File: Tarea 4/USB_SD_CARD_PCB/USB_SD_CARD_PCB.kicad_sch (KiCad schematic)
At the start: 3 parts

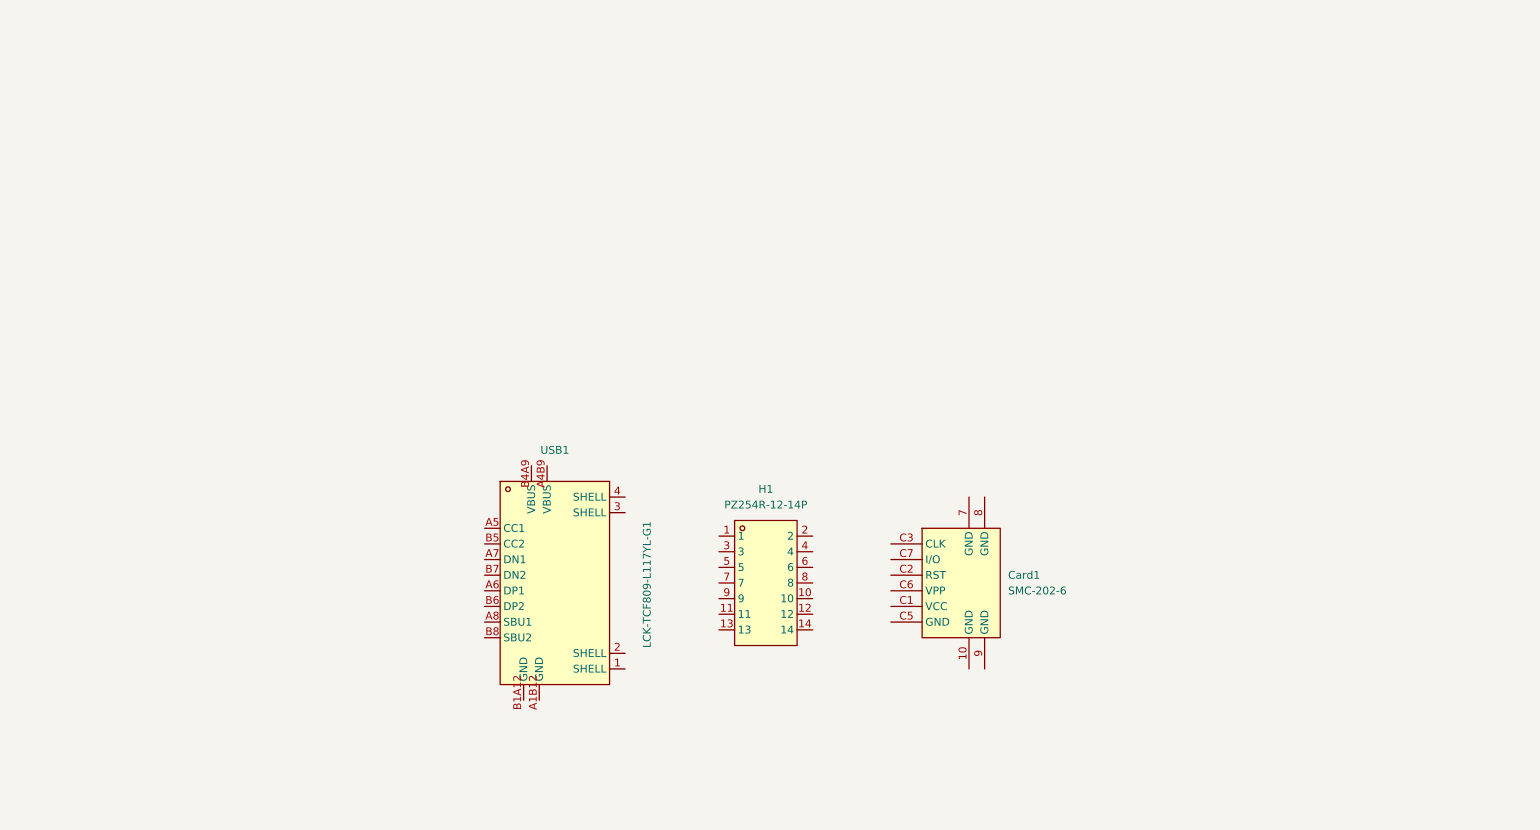
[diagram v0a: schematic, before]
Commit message: USB type c Conexiones
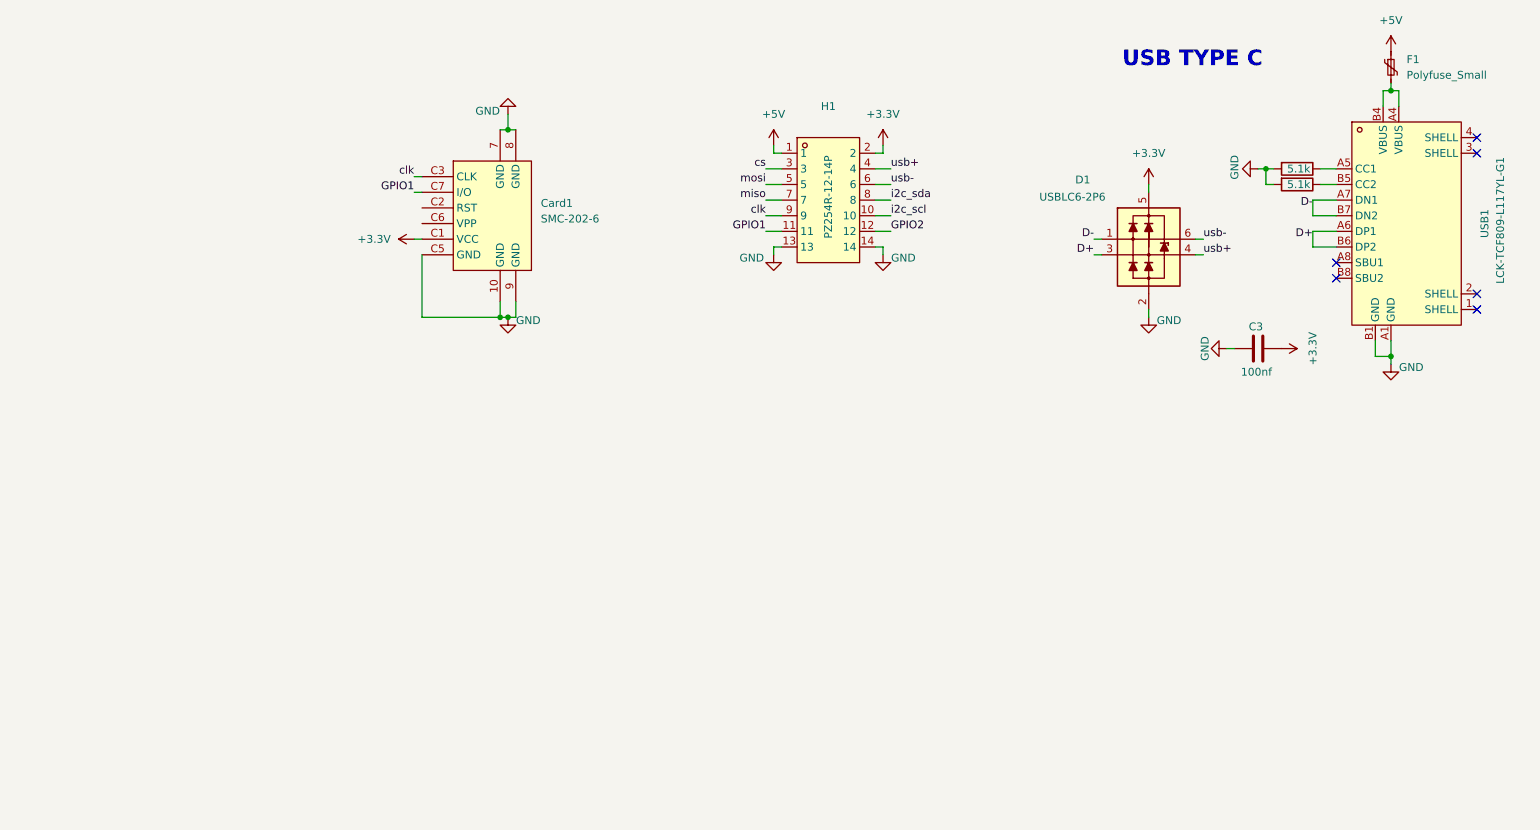
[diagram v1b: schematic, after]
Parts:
- added C3: 100nf, Capacitor_SMD:C_0805_2012Metric, symbol Device:C
- added D1: USBLC6-2P6, PCM_Package_TO_SOT_SMD_AKL:SOT-666, symbol PCM_Diode_TVS_AKL:USBLC6-2P6
- added F1: Polyfuse_Small, Fuse:Fuse_0805_2012Metric, symbol Device:Polyfuse_Small
- added R1, R2: 5.1k, Resistor_SMD:R_0805_2012Metric, symbol Device:R
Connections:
- net +5V: now reaches H1.1
- net +5V: now also F1.1
- net i2c_scl: now reaches H1.10
- net GPIO1: now reaches H1.11
- net GPIO1: now also Card1.C7 (I/O)
- net GPIO2: now reaches H1.12
- net GND: now reaches H1.13
- net GND: now also Card1.10 (GND), Card1.7 (GND), Card1.8 (GND), Card1.9 (GND), Card1.C5 (GND), H1.14, USB1.A1 (GND), USB1.B1 (GND), C3.2, D1.2 (VN), R1.2, R2.2
- net +3.3V: now reaches H1.2
- net +3.3V: now also Card1.C1 (VCC), C3.1, D1.5 (VP)
- net cs: now reaches H1.3
- net usb+: now reaches H1.4
- net usb+: now also D1.4 (L2)
- net mosi: now reaches H1.5
- net usb-: now reaches H1.6
- net usb-: now also D1.6 (L1)
- net miso: now reaches H1.7
- net i2c_sda: now reaches H1.8
- net clk: now reaches H1.9
- net clk: now also Card1.C3 (CLK)
- net at USB1.A5 (CC1): now also R1.1
- net D+: now reaches USB1.A6 (DP1)
- net D+: now also USB1.B6 (DP2), D1.3 (L2)
- net D-: now reaches USB1.A7 (DN1)
- net D-: now also USB1.B7 (DN2), D1.1 (L1)
- net at USB1.B5 (CC2): now also R2.1
- new net: F1.2, USB1.A4 (VBUS), USB1.B4 (VBUS)
- no-connect marks 0 -> 6
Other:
- note added: "USB TYPE C"
- moved on the sheet: Card1, H1, USB1

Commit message: USB CARD Y SD
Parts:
- removed Card1: SMC-202-6, EasyEDA:SIM-SMD_SMC-202-6, symbol EasyEDA:SMC-202-6
- removed H1: PZ254R-12-14P, EasyEDA:HDR-TH_14P-P2.54-H-M-R2-C7-S2.54, symbol EasyEDA:PZ254R-12-14P
- added C1: 100nf, Capacitor_SMD:C_0805_2012Metric, symbol Device:C
- added C2: 10uF, Capacitor_SMD_AKL:C_0603_1608Metric, symbol Capacitor_AKL:C_0603
- added Card2: TF-115, EasyEDA:TF-SMD_TF-115, symbol EasyEDA:TF-115
- added FPC1: FPC-05FB-30PH20, EasyEDA:FPC-SMD_30P-P0.50_FPC-05FB-30PH20, symbol EasyEDA:FPC-05FB-30PH20
- added J1: PZ254R-12-16P, EasyEDA:HDR-TH_16P-P2.54-H-M-R2-C8-S2.54, symbol EasyEDA:PZ254R-12-16P
- added R3, R4, R5, R6, R7: 10k, Resistor_SMD:R_0805_2012Metric, symbol Device:R
- added U1: MT9700-N, EasyEDA:SOT-23-5_L2.9-W1.6-P0.95-LS2.9-BL, symbol EasyEDA:MT9700-N
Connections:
- net +3.3V: now also C1.1, Card2.4 (VDD), FPC1.2, FPC1.25, J1.2, R3.1, R4.1, R5.1, R6.1
- net +5V: now also J1.1
- net GND: now also C1.2, C2.2, Card2.10 (SHELL), Card2.11 (SHELL), Card2.12 (SHELL), Card2.13 (SHELL), Card2.6 (VSS), FPC1.1, FPC1.21, FPC1.22, FPC1.23, FPC1.24, FPC1.30, FPC1.31, FPC1.32, J1.15, J1.16, R7.2, U1.2 (GND)
- net usb+ renamed USB+
- net USB+: now also J1.4
- net usb- renamed USB-
- net USB-: now also J1.6
- new net: C2.1, U1.1 (VOUT)
- new net: Card2.1 (DAT2), R3.2
- new net: Card2.8 (DAT1), R5.2
- new net I2C_SCK: FPC1.26, J1.10
- new net I2C_SDA: FPC1.27, J1.8
- new net IM1: FPC1.4
- new net IM2: FPC1.3
- new net LCD_CS: FPC1.6, J1.13
- new net LCD_EN: J1.12
- new net LED+: FPC1.20
- new net RESET: FPC1.29, FPC1.5, J1.11
- new net SD_CS: Card2.2 (CD/DAT3), J1.3, R4.2
- new net SPI_CLK: Card2.5 (CLK), J1.9
- new net SPI_MISO: Card2.7 (DAT0), J1.7, R6.2
- new net SPI_MOSI: Card2.3 (CMD), J1.5
- new net TP_INT: FPC1.28, J1.14
- no-connect marks 6 -> 15
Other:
- note added: "Connector"
- note added: "Connector LCD"
- note added: "MICROSD CARD"

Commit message: Actualizacion 18/04/26
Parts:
- added R10, R11, R9: 10K, PCM_Resistor_SMD_AKL:R_0603_1608Metric, symbol Device:R
- added R8: 300R, PCM_Resistor_SMD_AKL:R_0603_1608Metric, symbol Device:R
- C2: footprint Capacitor_SMD_AKL:C_0603_1608Metric -> Capacitor_SMD:C_0201_0603Metric
- R3, R4, R5, R6: footprint Resistor_SMD:R_0805_2012Metric -> PCM_Resistor_SMD_AKL:R_0603_1608Metric
- R7: value 10k -> 6.8K; footprint Resistor_SMD:R_0805_2012Metric -> PCM_Resistor_SMD_AKL:R_0603_1608Metric
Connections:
- net +3.3V: now also C2.1, U1.5 (VIN), R10.2, R11.2, R9.2; no longer FPC1.2
- net IM1: now also R11.1
- net IM2: now also R10.1
- net LCD_EN: now also U1.4 (EN)
- net LED+: now also R8.2
- net RESET: now also R9.1
- net VDD: now reaches U1.1 (VOUT)
- net VDD: now also FPC1.2, R8.1; no longer C2.1
- net at U1.3 (SET): now also R7.1
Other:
- moved on the sheet: C2, FPC1, U1
